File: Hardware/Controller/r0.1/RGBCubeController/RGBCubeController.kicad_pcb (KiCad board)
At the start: 4 copper layers, 61 x 61 mm, 97 parts, among them J1 Conn0, J2 Conn1, J3 Conn2, J4 JTAG, J5 UART, J6 Battery, Q1 AON7804, SW1 Reset, SW2 BTN0, SW3 BOOT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

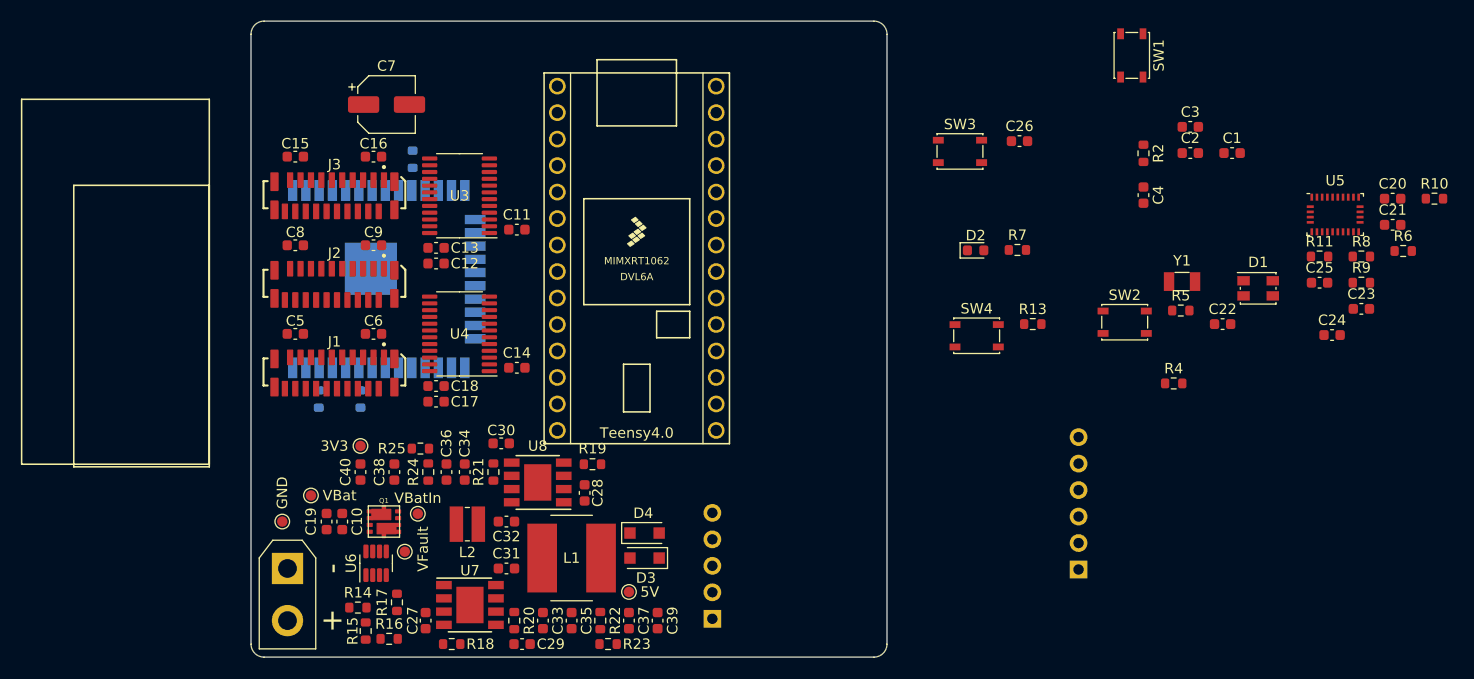
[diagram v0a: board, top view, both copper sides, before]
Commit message: [RGBCubeController] Switched to using the Unexpected Maker TinyS3 ESP32 S3 dev board. This removes the need for a 3V3 regulator, reduces the number of components, as well as improving the main microcontroller. It is more expensive, and also takes up more space. Currently parts are all placed on the board (except for the power switch), but no routing has been done.
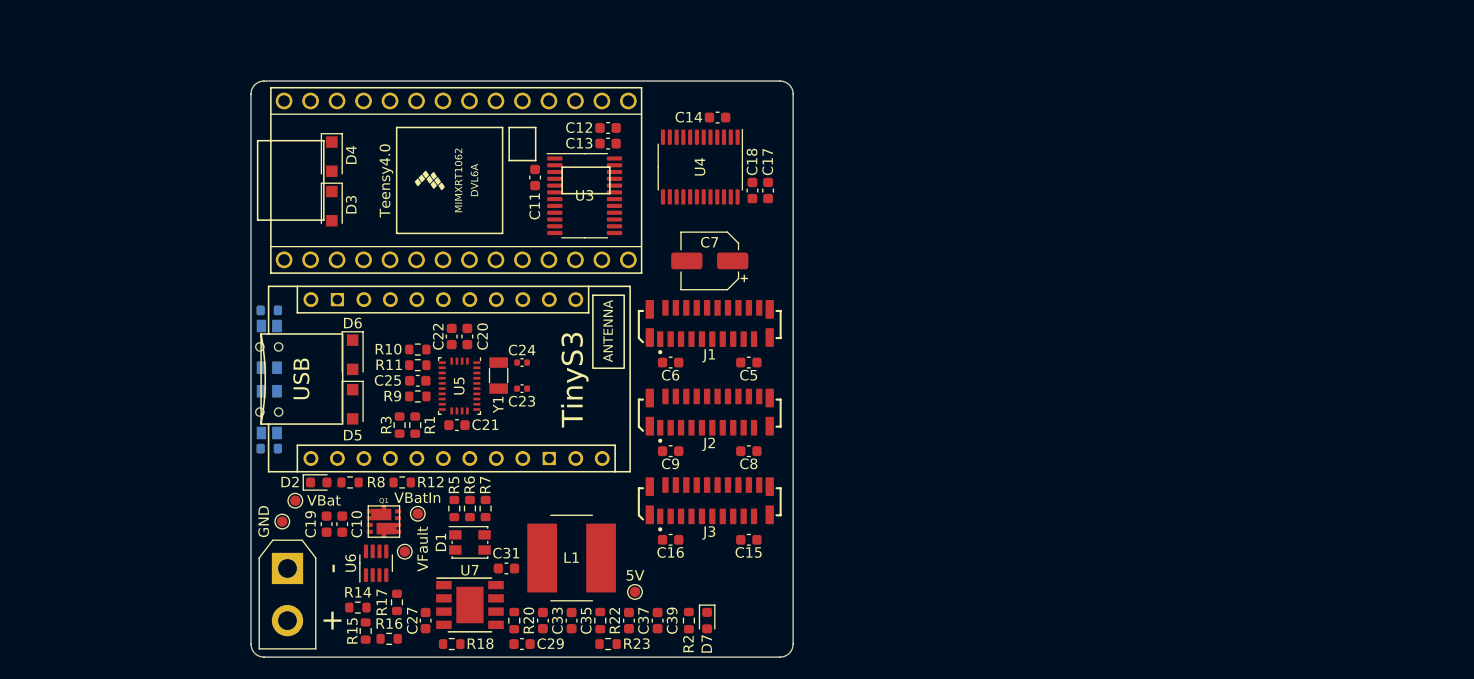
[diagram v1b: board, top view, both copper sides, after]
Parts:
- removed C1, C38, C40: 22μF, Capacitor_SMD:C_0603_1608Metric
- removed C2, C26, C3, C32: 100nF, Capacitor_SMD:C_0603_1608Metric
- removed C28: 10μF, Capacitor_SMD:C_0603_1608Metric
- removed C30: 3.3nF, Capacitor_SMD:C_0603_1608Metric
- removed C34: 68pF, Capacitor_SMD:C_0603_1608Metric
- removed C36: open, Capacitor_SMD:C_0603_1608Metric
- removed C4: 1μF, Capacitor_SMD:C_0603_1608Metric
- removed J4: JTAG, Connector_PinHeader_2.54mm:PinHeader_1x05_P2.54mm_Vertical
- removed J5: UART, Connector_PinHeader_2.54mm:PinHeader_1x06_P2.54mm_Horizontal
- removed L2: 4.7μH, Inductor_SMD:L_Wuerth_MAPI-3015
- removed R19: 200k, Resistor_SMD:R_0603_1608Metric
- removed R21: 9.31k, Resistor_SMD:R_0603_1608Metric
- removed R24: 69.6k, Resistor_SMD:R_0603_1608Metric
- removed R25: 22.1k, Resistor_SMD:R_0603_1608Metric
- removed SW1: Reset, Button_Switch_SMD:SW_SPST_PTS810
- removed SW3: BOOT, Button_Switch_SMD:SW_SPST_PTS810
- removed TP6: 3V3, TestPoint:TestPoint_Pad_D1.0mm
- removed U8: AP64350, Package_SO:Diodes_SO-8EP
- added D5: D_Schottky, Diode_SMD:D_SOD-123F, F.Cu at (109.8, 86.8)
- added D6: D_Schottky, Diode_SMD:D_SOD-123F, F.Cu at (109.8, 82.0)
- added D7: LED, LED_SMD:LED_0603_1608Metric, F.Cu at (143.8, 107.5)
- C23, C24: footprint Capacitor_SMD:C_0603_1608Metric -> Capacitor_SMD:C_0402_1005Metric
- R1, R12, R3: moved to F.Cu
- R13, R4: moved to B.Cu
- R2: value 10k -> 1k
- SW2, SW4: footprint Button_Switch_SMD:SW_SPST_PTS810 -> PTS841:PTS841_GKP; moved to B.Cu
- U1: value ESP32-WROOM-32UE -> TinyS3; footprint RF_Module:ESP32-WROOM-32U -> footprints:TinyS3; moved to F.Cu
- moved R8 99.4 mm to (109.5, 94.2), turned to 180 degrees
- moved R10 98.6 mm to (116.0, 81.5), turned to 180 degrees
- moved R6 92.9 mm to (121.0, 96.8), turned to -90 degrees
- moved C21 91.8 mm to (119.8, 88.8)
- moved R9 91.2 mm to (116.0, 86.0)
- moved C20 89.7 mm to (120.8, 80.2), turned to 90 degrees
- moved R11 87.1 mm to (116.0, 83.0), turned to 180 degrees
- moved C25 87.0 mm to (116.0, 84.5), turned to 180 degrees
- moved R4 87.0 mm to (101.8, 91.0), turned to 180 degrees
- moved U5 85.6 mm to (120.0, 85.0), turned to -90 degrees
- moved SW2 82.5 mm to (101.8, 87.5), turned to -90 degrees
- moved C23 80.9 mm to (126.0, 85.2)
- moved D1 79.4 mm to (121.0, 100.0)
- moved C24 77.7 mm to (126.0, 82.8)
- moved C22 73.9 mm to (119.2, 80.2), turned to 90 degrees
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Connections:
- net /TEENSY_VIN renamed /TEENSY_5V
- C11 pad 1: +3V3 -> /3V3_TEENSY
- C14 pad 1: +3V3 -> /3V3_TEENSY
- R2 pad 1: +3V3 -> +5V
- R2 pad 2: Net-(U1-EN) -> Net-(D7-A)
- U1 pad 1: GND -> unconnected-(U1-VBAT)
- U1 pad 10: /Driver_CS -> /LED_B
- U1 pad 11: /LED_R -> unconnected-(U1-IO0)
- U1 pad 12: /LED_G -> /UART_RX
- U1 pad 13: /TMS -> /UART_TX
- U1 pad 14: /TDI -> GND
- U1 pad 15: GND -> unconnected-(U1-RST)
- U1 pad 16: /TCK -> /ESP_IO6
- U1 pad 17: unconnected-(U1-SHD/SD2) -> /ESP_IO7
- U1 pad 18: unconnected-(U1-SWP/SD3) -> /SDA
- U1 pad 19: unconnected-(U1-SCS/CMD) -> /SCL
- U1 pad 2: +3V3 -> GND
- U1 pad 20: unconnected-(U1-SCK/CLK) -> /Driver_CS
- U1 pad 21: unconnected-(U1-SDO/SD0) -> /SCK
- U1 pad 22: unconnected-(U1-SDI/SD1) -> /MISO
- U1 pad 23: /TDO -> /MOSI
- U1 pad 3: Net-(U1-EN) -> /ESP_5V
- U1 pad 4: unconnected-(U1-SENSOR_VP) -> +3V3
- U1 pad 5: unconnected-(U1-SENSOR_VN) -> /BTN0
- U1 pad 6: /BTN0 -> /BTN1
- U1 pad 7: /BTN1 -> unconnected-(U1-IO3)
- U1 pad 8: /LED_B -> /LED_R
- U1 pad 9: unconnected-(U1-IO33) -> /LED_G
- U2 pad 31: unconnected-(U2-3V3) -> /3V3_TEENSY
- U3 pad 1: +3V3 -> /3V3_TEENSY
- U3 pad 2: +3V3 -> /3V3_TEENSY
- U4 pad 1: +3V3 -> /3V3_TEENSY
- U4 pad 2: +3V3 -> /3V3_TEENSY
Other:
- board size 61 x 61 mm -> 52 x 55.3 mm

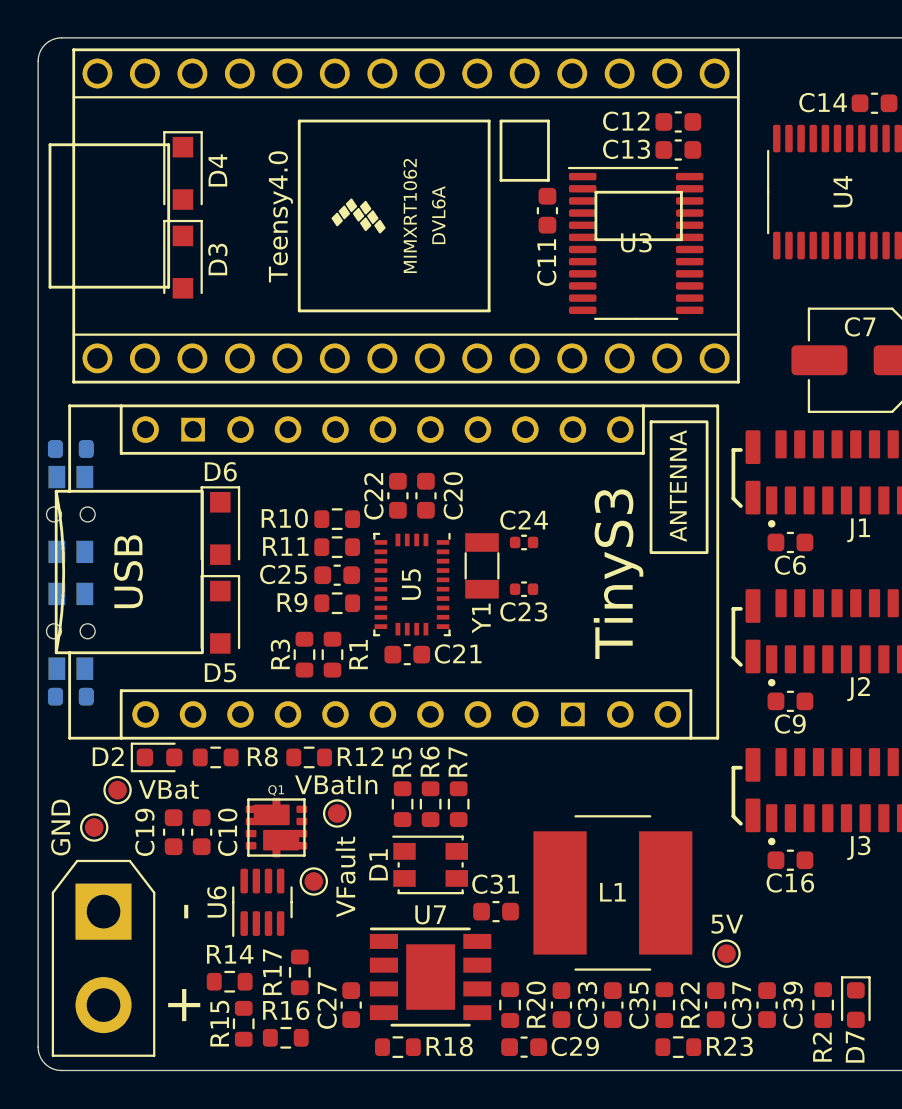
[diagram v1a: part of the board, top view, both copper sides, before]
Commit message: [RGBCubeController] Added power off switch. There will still be ~10 - 20uA current draw when off, so battery should be disconnected for long term storage. Still need to route everything.
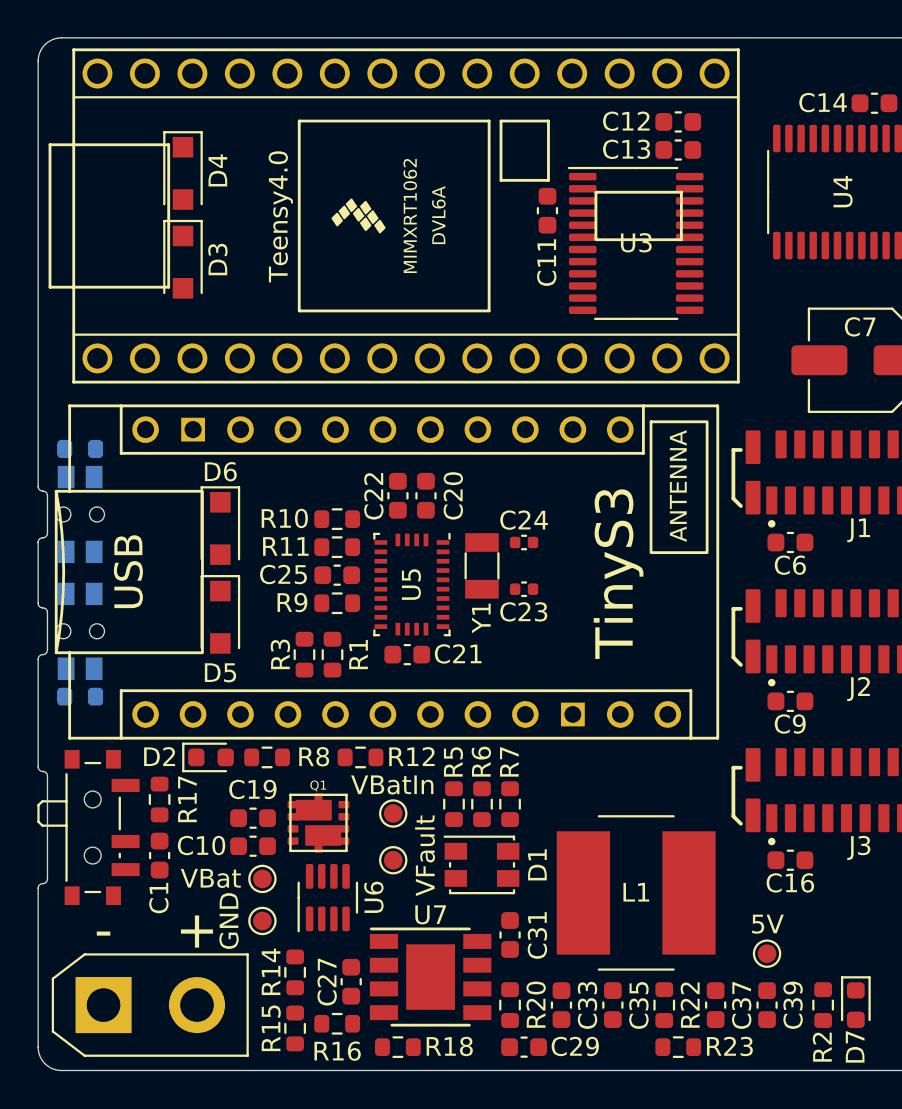
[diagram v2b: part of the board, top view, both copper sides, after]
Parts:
- added C1: 100nF, Capacitor_SMD:C_0603_1608Metric, F.Cu at (106.5, 99.5)
- added SW3: SW_SPDT, Button_Switch_SMD:SW_SPDT_PCM12, F.Cu at (103.2, 98.0)
- R17: value 182k -> 510k
- moved R17 11.9 mm to (106.5, 96.5), turned to -90 degrees
- moved TP1 10.3 mm to (112.0, 103.0)
- moved TP4 9.09 mm to (112.0, 100.8), turned to -90 degrees
- moved J6 5.00 mm to (103.5, 107.5), turned to 0 degrees
- moved TP3 4.40 mm to (119.0, 99.8)
- moved C19 4.32 mm to (111.5, 97.5), turned to 180 degrees
- moved R14 3.54 mm to (113.8, 105.8), turned to -90 degrees
- moved U6 3.51 mm to (115.5, 101.8)
- moved TP2 3.00 mm to (119.0, 97.2)
- moved C10 2.85 mm to (111.5, 99.0), turned to 180 degrees
- moved R16 2.85 mm to (116.0, 108.5)
- moved R15 2.76 mm to (113.8, 108.8)
- moved D1 2.75 mm to (123.8, 100.0)
- moved D2 2.75 mm to (109.2, 94.2)
- moved R12 2.75 mm to (117.2, 94.2)
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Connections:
- J6 pad 2: Net-(J6-Pin_2) -> Net-(Q1A-D)
- Q1 pad 1: Net-(J6-Pin_2) -> Net-(Q1A-D)
- R14 pad 1: Net-(J6-Pin_2) -> Net-(Q1A-D)
- R17 pad 1: Net-(J6-Pin_2) -> Net-(SW3-A)
- R17 pad 2: Net-(U6-~{SHDN}) -> Net-(Q1A-D)
- TP2 pad 1: Net-(J6-Pin_2) -> Net-(Q1A-D)
- U6 pad 1: Net-(J6-Pin_2) -> Net-(Q1A-D)
- U6 pad 5: Net-(U6-~{SHDN}) -> /Power/~{SHDN}
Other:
- outline, holes or cut-outs redrawn

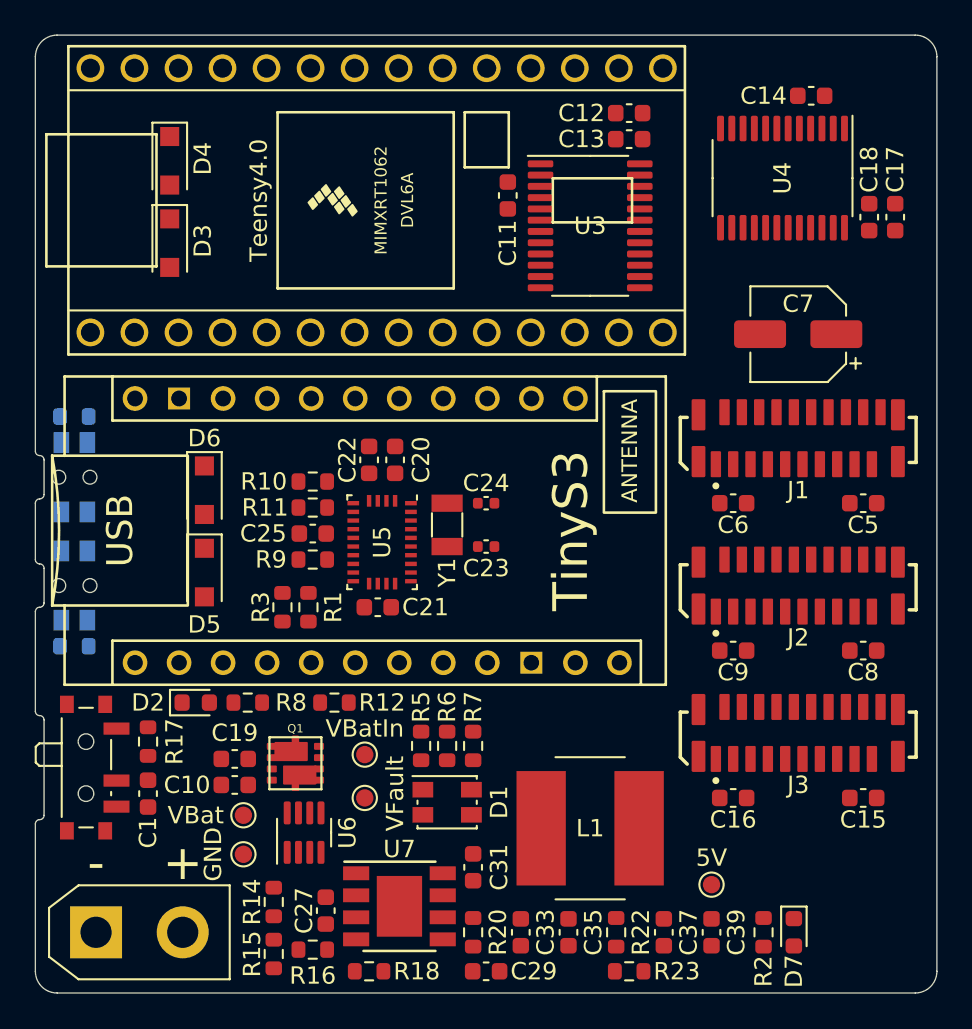
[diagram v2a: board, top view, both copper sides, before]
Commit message: [RGBCubeController] Added Qwiic connector, as well as a pattern to the silkscreen on backside of PCB.
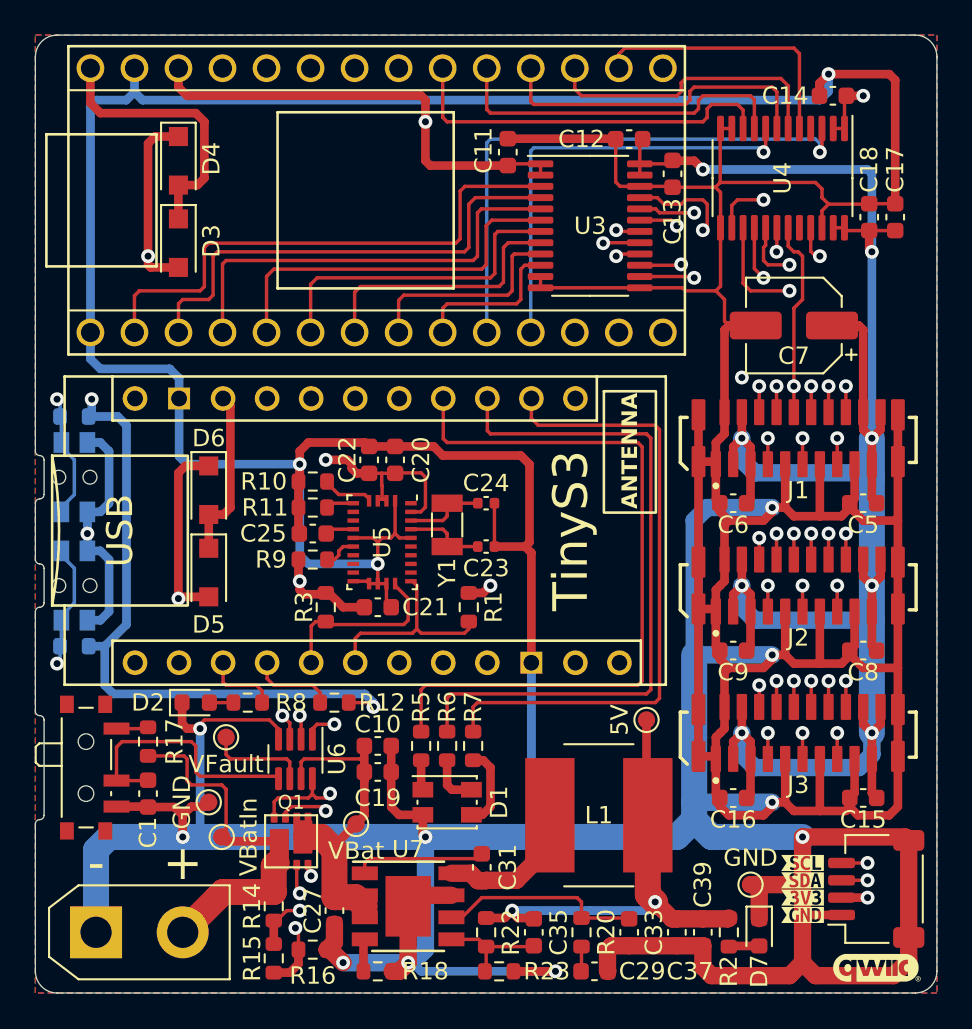
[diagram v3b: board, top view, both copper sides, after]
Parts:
- added G***: LOGO, SilkscreenPatterns:slime-mold-0, B.Cu at (126.0, 83.4)
- added G1: LOGO, Qwiic:Qwiic, F.Cu at (148.5, 109.5)
- added J4: Qwiic, Connector_JST:JST_SH_SM04B-SRSS-TB_1x04-1MP_P1.00mm_Horizontal, F.Cu at (148.5, 105.0)
- added TP6: GND, CustomTestPoint.pretty:TestPoint_Pad_D1.0mm, F.Cu at (141.2, 104.8)
- added kibuzzard-621A4989: G***, kibuzzard-621A4989, F.Cu at (144.2, 105.5)
- added kibuzzard-621A49AA: G***, kibuzzard-621A49AA, F.Cu at (144.2, 104.5)
- added kibuzzard-621A49B5: G***, kibuzzard-621A49B5, F.Cu at (144.2, 103.5)
- added kibuzzard-621A4C97: G***, kibuzzard-621A4C97, F.Cu at (144.2, 106.5)
- TP1, TP2, TP3, TP4, TP5: footprint TestPoint:TestPoint_Pad_D1.0mm -> CustomTestPoint.pretty:TestPoint_Pad_D1.0mm
- U6: footprint Package_TO_SOT_SMD:TSOT-23-8 -> TSOT:TSOT-23-8
- moved TP5 10.2 mm to (135.2, 95.2), turned to -90 degrees
- moved TP2 9.52 mm to (110.8, 102.0), turned to 90 degrees
- moved R1 9.25 mm to (125.0, 88.8)
- moved TP3 8.73 mm to (111.0, 96.2), turned to 0 degrees
- moved C10 8.55 mm to (119.8, 96.8), turned to 0 degrees
- moved C19 8.28 mm to (119.8, 98.2), turned to 0 degrees
- moved R22 7.50 mm to (126.0, 107.5)
- moved R23 7.50 mm to (126.8, 109.8)
- moved TP4 6.52 mm to (118.5, 101.2), turned to 0 degrees
- moved C29 6.25 mm to (132.2, 109.8)
- moved C33 6.25 mm to (134.2, 107.5)
- moved R20 6.25 mm to (131.5, 107.5)
- moved Q1 4.51 mm to (114.8, 102.2), turned to 90 degrees
- moved U6 4.28 mm to (115.0, 97.5), turned to -90 degrees
- moved TP1 3.61 mm to (110.0, 100.0), turned to -90 degrees
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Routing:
- net GND: track 0.00 -> 559.7 mm, vias 0 -> 14
- net +5V: track 0.00 -> 273.3 mm, vias 0 -> 12
- net +3V3: track 0.00 -> 132.9 mm, vias 0 -> 6
- net /SCK: track 0.00 -> 74.6 mm
- net /UART_TX: track 0.00 -> 64.1 mm
- net /UART_RX: track 0.00 -> 64.0 mm
- net /3V3_TEENSY: track 0.00 -> 56.6 mm, vias 0 -> 2
- net /SDA: track 0.00 -> 56.2 mm, vias 0 -> 1
- net /SCL: track 0.00 -> 54.6 mm, vias 0 -> 1
- net /Conn_Latch: track 0.00 -> 54.4 mm, vias 0 -> 4
- net /MOSI: track 0.00 -> 52.2 mm
- net /Driver_CS: track 0.00 -> 51.2 mm
- net /Conn_RowLatch: track 0.00 -> 49.4 mm, vias 0 -> 4
- net /MISO: track 0.00 -> 48.3 mm
- net Net-(J6-Pin_2): track 0.00 -> 43.9 mm, vias 0 -> 1
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- added copper zone on B.Cu, net GND
- added copper zone on F.Cu, net GND
